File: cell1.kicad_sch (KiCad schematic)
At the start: 0 parts

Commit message: Added a few more components to the sch
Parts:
- added BT1: Battery_Cell, symbol Device:Battery_Cell
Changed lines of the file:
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@@
 	(generator_version "8.0")
 	(paper "A4")
+	(symbol
+		(lib_id "Device:Battery_Cell")
+		(at 154.94 106.68 0)
+		(unit 1)
+		(exclude_from_sim no)
+		(in_bom yes)
+		(on_board yes)
+		(dnp no)
+		(fields_autoplaced yes)
+		(property "Reference" "BT1"
+			(at 158.75 103.5684 0)
+			(effects
+				(font
+					(size 1.27 1.27)
+				)
+				(justify left)
+			)
+		)
+		(property "Value" "Battery_Cell"
+			(at 158.75 106.1084 0)
+			(effects
+				(font
+					(size 1.27 1.27)
+				)
+				(justify left)
+			)
+		)
+		(property "Footprint" ""
+			(at 154.94 105.156 90)
+			(effects
+				(font
+					(size 1.27 1.27)
+				)
+				(hide yes)
+			)
+		)
+		(property "Datasheet" "~"
+			(at 154.94 105.156 90)
+			(effects
+				(font
+					(size 1.27 1.27)
+				)
+				(hide yes)
+			)
+		)
+		(property "Description" "Single-cell battery"
+			(at 154.94 106.68 0)
+			(effects
+				(font
+					(size 1.27 1.27)
+				)
+				(hide yes)
+			)
+		)
+		(pin "2"
+		)
+		(pin "1"
+		)
+		(instances
+			(project "Cell-Characterization-Board"
+				(path "/8cf78a1b-eb7a-4166-aa75-ad898a030304/38288aa7-9276-4cb3-98d9-ec0b89c88535"
+					(reference "BT1")
+					(unit 1)
+				)
+			)
+		)
+	)
 )

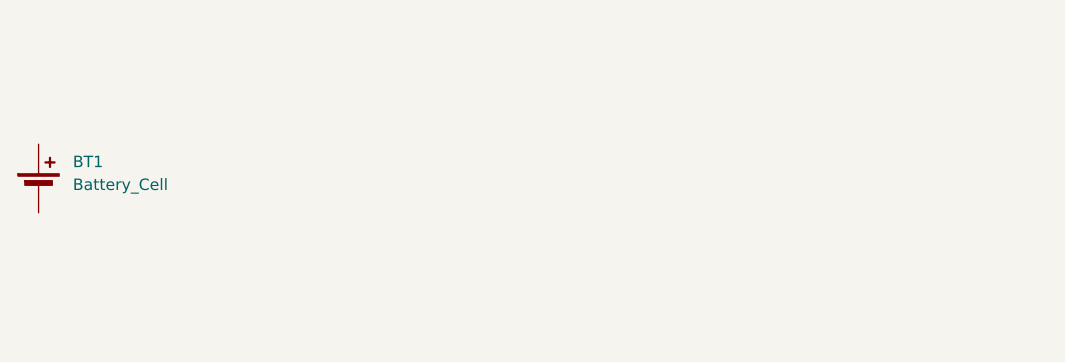
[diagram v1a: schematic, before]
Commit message: Finished Micro USB UART Bridge, started working on cell sch
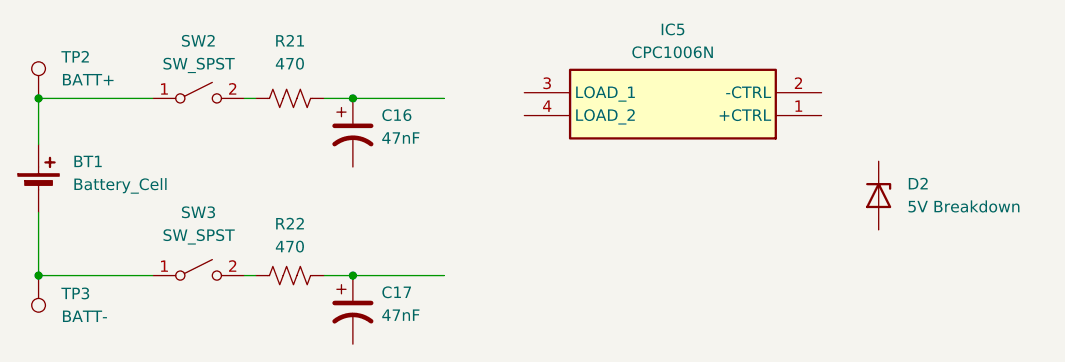
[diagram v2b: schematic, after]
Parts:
- added C16, C17: 47nF, symbol Device:C_Polarized_US
- added D2: 5V Breakdown, symbol Device:D_Zener
- added IC5: CPC1006N, SOP254P610X216-4N, symbol CPC1006N:CPC1006N
- added R21, R22: 470, symbol Device:R_US
- added SW2, SW3: SW_SPST, symbol Switch:SW_SPST
- added TP2: BATT+, symbol Connector:TestPoint
- added TP3: BATT-, symbol Connector:TestPoint
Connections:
- net at BT1.1 (+): now also SW2.1 (A), TP2.1
- net at BT1.2 (-): now also SW3.1 (A), TP3.1
- new net: R22.1, SW3.2 (B)
- new net: C17.1, R22.2
- new net: C16.1, R21.2
- new net: R21.1, SW2.2 (B)

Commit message: updated cell
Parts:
- removed D2: 5V Breakdown, symbol Device:D_Zener
- removed IC5: CPC1006N, SOP254P610X216-4N, symbol CPC1006N:CPC1006N
- added C18: 47nF, symbol Device:C_Polarized_US
- added D2: SBR10E45P5-7, SBR10E45P57, symbol SBR10E45P5-7:SBR10E45P5-7
- added D3, D4: 1N4448W, Diode_SMD:D_SOD-123, symbol Diode:1N4448W
- added F1: Fuse, symbol Device:Fuse
- added K1: V23105A5001A201, V23105A5001A201, symbol V23105A5001A201:V23105A5001A201
- added Q4: IRLML0030, Package_TO_SOT_SMD:SOT-23, symbol Transistor_FET:IRLML0030
- added R23: 20m, symbol Device:R_US
- added R26: 10k, symbol Device:R_US
- TP2: value BATT+ -> BATT1+
- TP3: value BATT- -> BATT1-
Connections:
- net Batt+: now reaches BT1.1 (+), SW2.1 (A), TP2.1
- net Batt+: now also K1.13
- net Batt1+: now reaches C17.1, R22.2
- net Batt-: now reaches BT1.2 (-), SW3.1 (A), TP3.1
- net Batt-: now also K1.4
- net GND: now reaches C17.2
- net GND: now also C16.2, K1.6, Q4.2 (S), R26.2
- net Batt1-: now reaches C16.1, R21.2
- new net: D3.2 (A), K1.1, Q4.3 (D)
- new net: D3.1 (K), D4.1 (K), K1.16
- new net: D2.3 (K), F1.1
- new net +5V: D4.2 (A), K1.9
- new net Curr_Sense1+: C18.1, F1.2, R23.1
- new net Curr_Sense1-: C18.2, R23.2
- new net REL_OUT: D2.1 (A_1), D2.2 (A_2), K1.11, K1.8
- new net Relay1: Q4.1 (G), R26.1
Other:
- note added: "CELL & ADC"
- note added: "CHARGE/DISCHARGE RELAY"
- moved on the sheet: BT1, C16, C17, R21, R22, SW2, SW3, TP2, TP3
